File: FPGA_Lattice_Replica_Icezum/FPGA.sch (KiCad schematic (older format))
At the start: 33 parts, among them U1 iCE40HX1K-TQ144, U2 N25Q032A

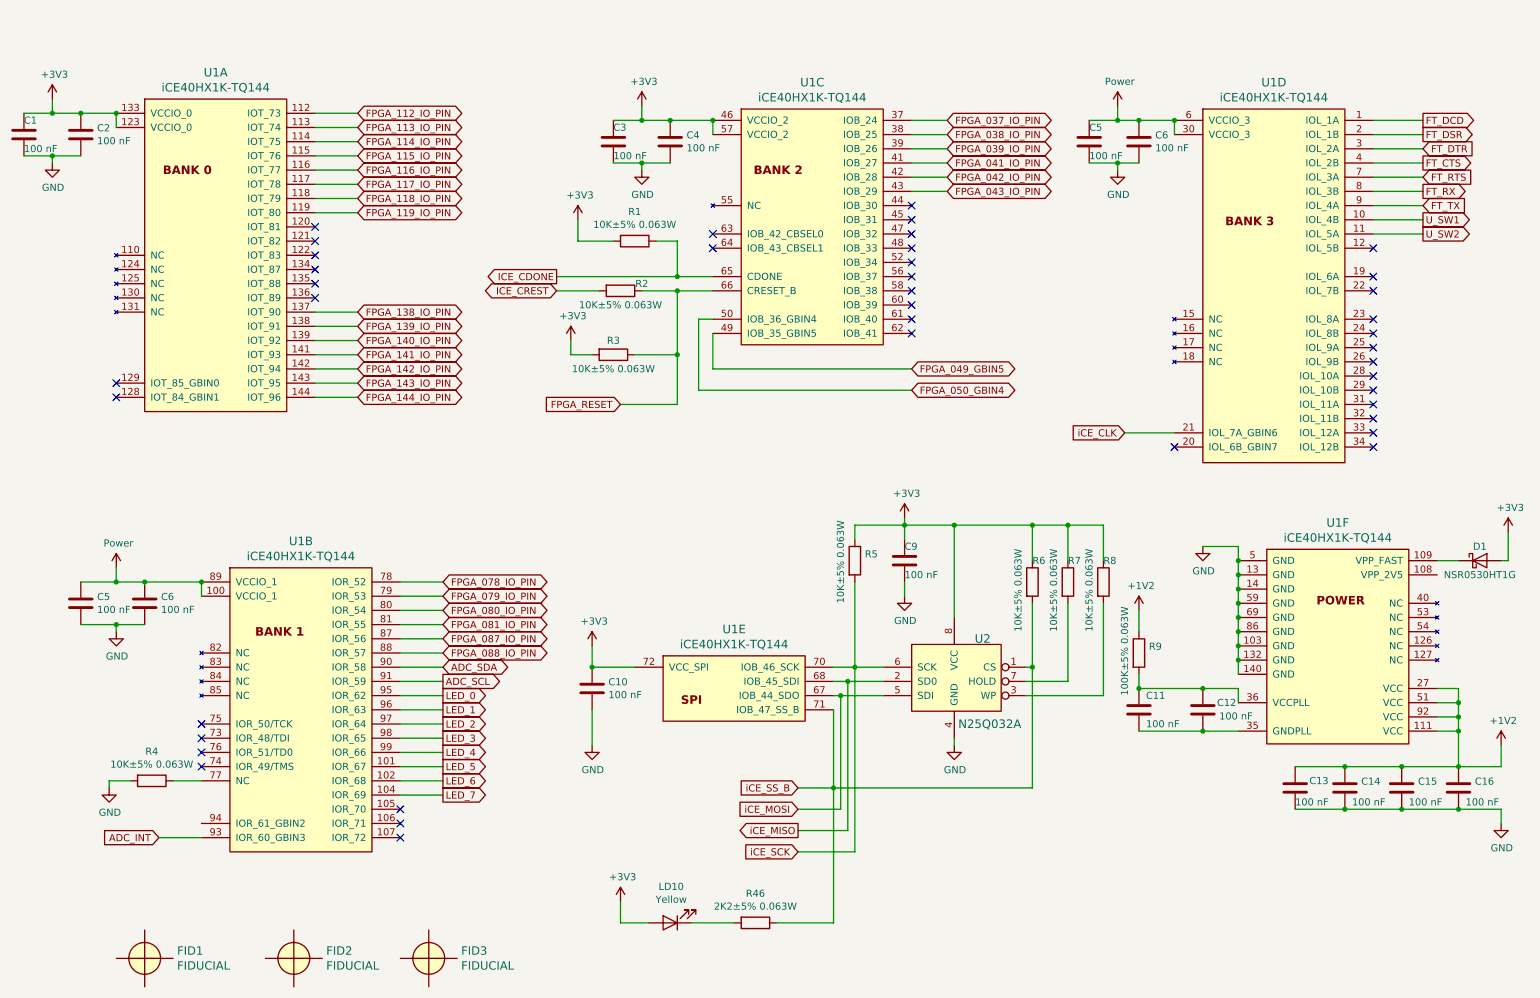
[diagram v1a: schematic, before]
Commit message: se ejecuto y se corrigio electrical rules check
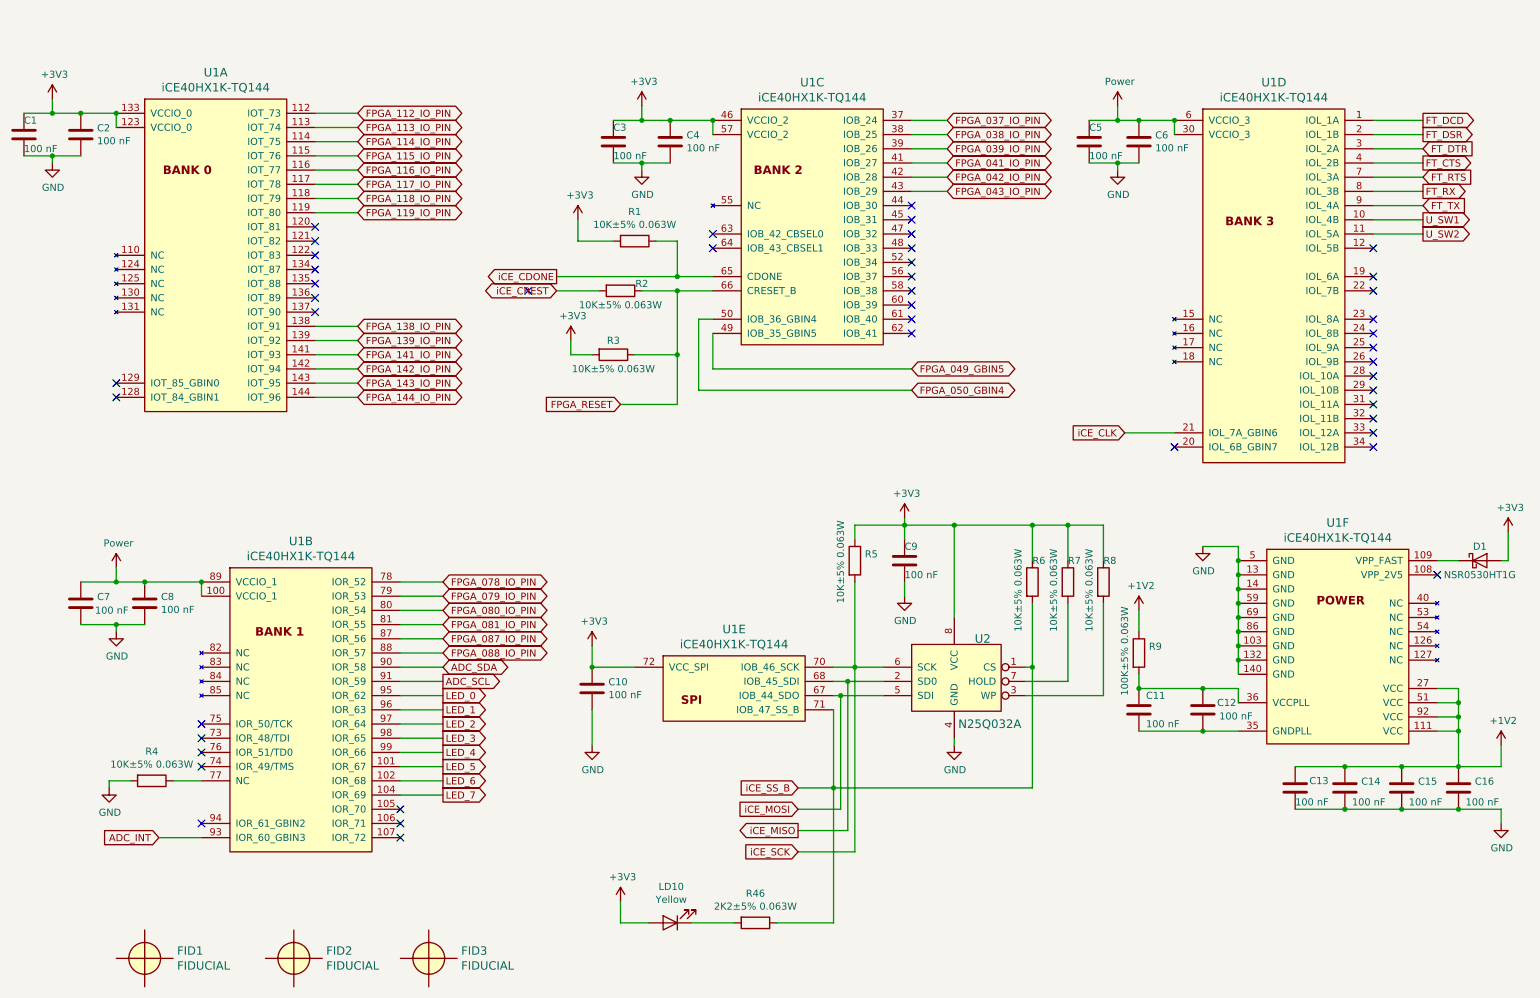
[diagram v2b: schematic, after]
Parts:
- renumbered C5 to C7, C6 to C8
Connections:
- net FPGA_140_IO_PIN is gone; now on net FPGA_139_IO_PIN: U1.139 (IOT_92)
- net FPGA_138_IO_PIN: now also U1.138 (IOT_91); no longer U1.137 (IOT_90)
- net FPGA_139_IO_PIN: no longer U1.138 (IOT_91)
- net ICE_CDONE renamed iCE_CDONE
- net ICE_CREST renamed iCE_CREST
- no-connect marks 41 -> 45
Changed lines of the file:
@@
 Text GLabel 2950 2000 2    50   BiDi ~ 0
 FPGA_119_IO_PIN
-Text GLabel 2950 2700 2    50   BiDi ~ 0
+Text GLabel 2950 2800 2    50   BiDi ~ 0
 FPGA_138_IO_PIN
-Text GLabel 2950 2800 2    50   BiDi ~ 0
+Text GLabel 2950 2900 2    50   BiDi ~ 0
 FPGA_139_IO_PIN
-Text GLabel 2950 2900 2    50   BiDi ~ 0
-FPGA_140_IO_PIN
 Text GLabel 2950 3000 2    50   BiDi ~ 0
 FPGA_141_IO_PIN
@@
 ADC_INT
 $Comp
-L icezum:Power #PWR?
+L icezum:Power #PWR0125
 U 1 1 5CFD3F9F
 P 1250 4500
-F 0 "#PWR?" H 1250 4350 50  0001 C CNN
+F 0 "#PWR0125" H 1250 4350 50  0001 C CNN
 F 1 "Power" H 1265 4673 50  0000 C CNN
 F 2 "" H 1250 4500 60  0000 C CNN
@@
 $EndComp
 $Comp
-L Device:C C5
+L Device:C C7
 U 1 1 5CFD4A6A
 P 1000 4750
-F 0 "C5" H 1115 4796 50  0000 L CNN
-F 1 "100 nF" H 1115 4705 50  0000 L CNN
+F 0 "C7" H 1115 4796 50  0000 L CNN
+F 1 "100 nF" H 1100 4700 50  0000 L CNN
 F 2 "" H 1038 4600 50  0001 C CNN
 F 3 "~" H 1000 4750 50  0001 C CNN
@@
 $EndComp
 $Comp
-L Device:C C6
+L Device:C C8
 U 1 1 5CFD4C0A
 P 1450 4750
-F 0 "C6" H 1565 4796 50  0000 L CNN
+F 0 "C8" H 1565 4796 50  0000 L CNN
 F 1 "100 nF" H 1565 4705 50  0000 L CNN
 F 2 "" H 1488 4600 50  0001 C CNN
@@
 FPGA_RESET
 Text GLabel 4350 2550 0    50   BiDi ~ 0
-ICE_CREST
+iCE_CREST
 Text GLabel 4350 2450 0    50   Output ~ 0
-ICE_CDONE
+iCE_CDONE
 $Comp
 L Device:R R2
@@
 $EndComp
 $Comp
-L icezum:+3V3 #PWR?
+L icezum:+3V3 #PWR0126
 U 1 1 5CFF6677
 P 6800 4150
-F 0 "#PWR?" H 6800 4000 50  0001 C CNN
+F 0 "#PWR0126" H 6800 4000 50  0001 C CNN
 F 1 "+3V3" H 6815 4323 50  0000 C CNN
 F 2 "" H 6800 4150 60  0000 C CNN
@@
 $EndComp
 $Comp
-L icezum:+3V3 #PWR?
+L icezum:+3V3 #PWR0127
 U 1 1 5CFF66F2
 P 4600 5050
-F 0 "#PWR?" H 4600 4900 50  0001 C CNN
+F 0 "#PWR0127" H 4600 4900 50  0001 C CNN
 F 1 "+3V3" H 4615 5223 50  0000 C CNN
 F 2 "" H 4600 5050 60  0000 C CNN
@@
 $EndComp
 $Comp
-L icezum:+3V3 #PWR?
+L icezum:+3V3 #PWR0128
 U 1 1 5CFF6BF1
 P 4800 6850
-F 0 "#PWR?" H 4800 6700 50  0001 C CNN
+F 0 "#PWR0128" H 4800 6700 50  0001 C CNN
 F 1 "+3V3" H 4815 7023 50  0000 C CNN
 F 2 "" H 4800 6850 60  0000 C CNN
@@
 iCE_SCK
 $Comp
-L power:GND #PWR?
+L power:GND #PWR0129
 U 1 1 5CFFACE6
 P 4600 5750
-F 0 "#PWR?" H 4600 5500 50  0001 C CNN
+F 0 "#PWR0129" H 4600 5500 50  0001 C CNN
 F 1 "GND" H 4605 5577 50  0000 C CNN
 F 2 "" H 4600 5750 50  0001 C CNN
@@
 $EndComp
 $Comp
-L power:GND #PWR?
+L power:GND #PWR0130
 U 1 1 5CFFB30C
 P 7150 5750
-F 0 "#PWR?" H 7150 5500 50  0001 C CNN
+F 0 "#PWR0130" H 7150 5500 50  0001 C CNN
 F 1 "GND" H 7155 5577 50  0000 C CNN
 F 2 "" H 7150 5750 50  0001 C CNN
@@
 $EndComp
 $Comp
-L power:GND #PWR?
+L power:GND #PWR0131
 U 1 1 5CFFCC0F
 P 6800 4700
-F 0 "#PWR?" H 6800 4450 50  0001 C CNN
+F 0 "#PWR0131" H 6800 4450 50  0001 C CNN
 F 1 "GND" H 6805 4527 50  0000 C CNN
 F 2 "" H 6800 4700 50  0001 C CNN
@@
 Connection ~ 1850 4600
 $Comp
-L power:GND #PWR?
+L power:GND #PWR0132
 U 1 1 5D03650F
 P 1250 4950
-F 0 "#PWR?" H 1250 4700 50  0001 C CNN
+F 0 "#PWR0132" H 1250 4700 50  0001 C CNN
 F 1 "GND" H 1255 4777 50  0000 C CNN
 F 2 "" H 1250 4950 50  0001 C CNN
@@
 	1250 4600 1450 4600
 $Comp
-L power:GND #PWR?
+L power:GND #PWR0133
 U 1 1 5D03AF49
 P 800 1650
-F 0 "#PWR?" H 800 1400 50  0001 C CNN
+F 0 "#PWR0133" H 800 1400 50  0001 C CNN
 F 1 "GND" H 805 1477 50  0000 C CNN
 F 2 "" H 800 1650 50  0001 C CNN
@@
 Wire Wire Line
 	2950 2000 2650 2000
-Wire Wire Line
-	2650 2700 2950 2700
 Wire Wire Line
 	2950 2800 2650 2800
@@
 	7100 1850 6850 1850
 $Comp
-L icezum:+3V3 #PWR?
+L icezum:+3V3 #PWR0134
 U 1 1 5D097DA0
 P 4500 2050
-F 0 "#PWR?" H 4500 1900 50  0001 C CNN
+F 0 "#PWR0134" H 4500 1900 50  0001 C CNN
 F 1 "+3V3" H 4515 2223 50  0000 C CNN
 F 2 "" H 4500 2050 60  0000 C CNN
@@
 	5200 2450 4350 2450
 $Comp
-L icezum:+3V3 #PWR?
+L icezum:+3V3 #PWR0135
 U 1 1 5D0ACF52
 P 4450 2900
-F 0 "#PWR?" H 4450 2750 50  0001 C CNN
+F 0 "#PWR0135" H 4450 2750 50  0001 C CNN
 F 1 "+3V3" H 4465 3073 50  0000 C CNN
 F 2 "" H 4450 2900 60  0000 C CNN
@@
 	5350 3250 6850 3250
 $Comp
-L power:GND #PWR?
+L power:GND #PWR0136
 U 1 1 5D0DDC54
 P 4950 1700
-F 0 "#PWR?" H 4950 1450 50  0001 C CNN
+F 0 "#PWR0136" H 4950 1450 50  0001 C CNN
 F 1 "GND" H 4955 1527 50  0000 C CNN
 F 2 "" H 4950 1700 50  0001 C CNN
@@
 $EndComp
 $Comp
-L power:GND #PWR?
+L power:GND #PWR0137
 U 1 1 5D18225B
 P 1200 6050
-F 0 "#PWR?" H 1200 5800 50  0001 C CNN
+F 0 "#PWR0137" H 1200 5800 50  0001 C CNN
 F 1 "GND" H 1205 5877 50  0000 C CNN
 F 2 "" H 1200 6050 50  0001 C CNN
@@
 $EndComp
 $Comp
-L icezum:Power #PWR?
+L icezum:Power #PWR0138
 U 1 1 5D192FB9
 P 8300 1250
-F 0 "#PWR?" H 8300 1100 50  0001 C CNN
+F 0 "#PWR0138" H 8300 1100 50  0001 C CNN
 F 1 "Power" H 8315 1423 50  0000 C CNN
 F 2 "" H 8300 1250 60  0000 C CNN
@@
 $EndComp
 $Comp
-L power:GND #PWR?
+L power:GND #PWR0139
 U 1 1 5D193C6D
 P 8300 1700
-F 0 "#PWR?" H 8300 1450 50  0001 C CNN
+F 0 "#PWR0139" H 8300 1450 50  0001 C CNN
 F 1 "GND" H 8305 1527 50  0000 C CNN
 F 2 "" H 8300 1700 50  0001 C CNN
@@
 Connection ~ 8700 1350
 $Comp
-L power:GND #PWR?
+L power:GND #PWR0140
 U 1 1 5D1C44B0
 P 8900 4350
-F 0 "#PWR?" H 8900 4100 50  0001 C CNN
+F 0 "#PWR0140" H 8900 4100 50  0001 C CNN
 F 1 "GND" H 8905 4177 50  0000 C CNN
 F 2 "" H 8900 4350 50  0001 C CNN
@@
 $EndComp
 $Comp
-L icezum:+1V2 #PWR?
+L icezum:+1V2 #PWR0141
 U 1 1 5D1C6F5E
 P 8450 4800
-F 0 "#PWR?" H 8450 4650 50  0001 C CNN
+F 0 "#PWR0141" H 8450 4650 50  0001 C CNN
 F 1 "+1V2" H 8465 4973 50  0000 C CNN
 F 2 "" H 8450 4800 60  0000 C CNN
@@
 $EndComp
 $Comp
-L power:GND #PWR?
+L power:GND #PWR0142
 U 1 1 5D1C9C8A
 P 11000 6300
-F 0 "#PWR?" H 11000 6050 50  0001 C CNN
+F 0 "#PWR0142" H 11000 6050 50  0001 C CNN
 F 1 "GND" H 11005 6127 50  0000 C CNN
 F 2 "" H 11000 6300 50  0001 C CNN
@@
 $EndComp
 $Comp
-L icezum:+1V2 #PWR?
+L icezum:+1V2 #PWR0143
 U 1 1 5D1CAE01
 P 11000 5750
-F 0 "#PWR?" H 11000 5600 50  0001 C CNN
+F 0 "#PWR0143" H 11000 5600 50  0001 C CNN
 F 1 "+1V2" H 11015 5923 50  0000 C CNN
 F 2 "" H 11000 5750 60  0000 C CNN
@@
 $EndComp
 $Comp
-L icezum:+3V3 #PWR?
+L icezum:+3V3 #PWR0144
 U 1 1 5D1CCFC9
 P 11050 4250
-F 0 "#PWR?" H 11050 4100 50  0001 C CNN
+F 0 "#PWR0144" H 11050 4100 50  0001 C CNN
 F 1 "+3V3" H 11065 4423 50  0000 C CNN
 F 2 "" H 11050 4250 60  0000 C CNN
@@
 	1    0    0    -1
 $EndComp
+NoConn ~ 2650 2700
+NoConn ~ 4150 2550
+NoConn ~ 10550 4550
+NoConn ~ 1850 6300
 $EndSCHEMATC

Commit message: se comenzo asignacion de footprints
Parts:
- C1, C10, C2, C3, C4, C5, C6, C7, C8, C9: footprint (none) -> footprints:C_0402
- C11: footprint (none) -> footprints:C_0603
- D1: footprint (none) -> footprints:SOD-323
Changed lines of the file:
@@
 F 0 "U1" H 1950 1587 60  0000 C CNN
 F 1 "iCE40HX1K-TQ144" H 1950 1481 60  0000 C CNN
-F 2 "" H 1600 100 60  0000 C CNN
+F 2 "" H 1600 100 60  0001 C CNN
 F 3 "" H 1600 100 60  0000 C CNN
 	1    1250 1300
@@
 F 0 "U1" H 2550 4887 60  0000 C CNN
 F 1 "iCE40HX1K-TQ144" H 2550 4781 60  0000 C CNN
-F 2 "" H 2200 3400 60  0000 C CNN
+F 2 "" H 2200 3400 60  0001 C CNN
 F 3 "" H 2200 3400 60  0000 C CNN
 	2    1850 4600
@@
 F 0 "U1" H 6150 1617 60  0000 C CNN
 F 1 "iCE40HX1K-TQ144" H 6150 1511 60  0000 C CNN
-F 2 "" H 5800 150 60  0000 C CNN
+F 2 "" H 5800 150 60  0001 C CNN
 F 3 "" H 5800 150 60  0000 C CNN
 	3    5450 1350
@@
 F 0 "U1" H 9400 1617 60  0000 C CNN
 F 1 "iCE40HX1K-TQ144" H 9400 1511 60  0000 C CNN
-F 2 "" H 9050 150 60  0000 C CNN
+F 2 "" H 9050 150 60  0001 C CNN
 F 3 "" H 9050 150 60  0000 C CNN
 	4    8700 1350
@@
 F 0 "U1" H 5600 5467 60  0000 C CNN
 F 1 "iCE40HX1K-TQ144" H 5600 5361 60  0000 C CNN
-F 2 "" H 5250 4000 60  0000 C CNN
+F 2 "" H 5250 4000 60  0001 C CNN
 F 3 "" H 5250 4000 60  0000 C CNN
 	5    4900 5200
@@
 F 0 "U1" H 9850 4717 60  0000 C CNN
 F 1 "iCE40HX1K-TQ144" H 9850 4611 60  0000 C CNN
-F 2 "" H 9500 3250 60  0000 C CNN
+F 2 "" H 9500 3250 60  0001 C CNN
 F 3 "" H 9500 3250 60  0000 C CNN
 	6    9150 4450
@@
 F 0 "C1" H 600 1550 50  0000 L CNN
 F 1 "100 nF" H 600 1350 50  0000 L CNN
-F 2 "" H 638 1300 50  0001 C CNN
+F 2 "footprints:C_0402" H 638 1300 50  0001 C CNN
 F 3 "~" H 600 1450 50  0001 C CNN
 	1    600  1450
@@
 F 0 "C2" H 1115 1496 50  0000 L CNN
 F 1 "100 nF" H 1115 1405 50  0000 L CNN
-F 2 "" H 1038 1300 50  0001 C CNN
+F 2 "footprints:C_0402" H 1038 1300 50  0001 C CNN
 F 3 "~" H 1000 1450 50  0001 C CNN
 	1    1000 1450
@@
 F 0 "C3" H 4750 1600 50  0000 L CNN
 F 1 "100 nF" H 4750 1400 50  0000 L CNN
-F 2 "" H 4788 1350 50  0001 C CNN
+F 2 "footprints:C_0402" H 4788 1350 50  0001 C CNN
 F 3 "~" H 4750 1500 50  0001 C CNN
 	1    4750 1500
@@
 F 0 "C4" H 5265 1546 50  0000 L CNN
 F 1 "100 nF" H 5265 1455 50  0000 L CNN
-F 2 "" H 5188 1350 50  0001 C CNN
+F 2 "footprints:C_0402" H 5188 1350 50  0001 C CNN
 F 3 "~" H 5150 1500 50  0001 C CNN
 	1    5150 1500
@@
 F 0 "C7" H 1115 4796 50  0000 L CNN
 F 1 "100 nF" H 1100 4700 50  0000 L CNN
-F 2 "" H 1038 4600 50  0001 C CNN
+F 2 "footprints:C_0402" H 1038 4600 50  0001 C CNN
 F 3 "~" H 1000 4750 50  0001 C CNN
 	1    1000 4750
@@
 F 0 "C8" H 1565 4796 50  0000 L CNN
 F 1 "100 nF" H 1565 4705 50  0000 L CNN
-F 2 "" H 1488 4600 50  0001 C CNN
+F 2 "footprints:C_0402" H 1488 4600 50  0001 C CNN
 F 3 "~" H 1450 4750 50  0001 C CNN
 	1    1450 4750
@@
 F 0 "U2" H 7350 5400 60  0000 C CNN
 F 1 "N25Q032A" H 7400 4800 60  0000 C CNN
-F 2 "" H 7180 5300 60  0000 C CNN
+F 2 "" H 7180 5300 60  0001 C CNN
 F 3 "" H 7180 5300 60  0000 C CNN
 	1    6650 5200
@@
 F 0 "C10" H 4715 5396 50  0000 L CNN
 F 1 "100 nF" H 4715 5305 50  0000 L CNN
-F 2 "" H 4638 5200 50  0001 C CNN
+F 2 "footprints:C_0402" H 4638 5200 50  0001 C CNN
 F 3 "~" H 4600 5350 50  0001 C CNN
 	1    4600 5350
@@
 F 0 "C9" H 6800 4550 50  0000 L CNN
 F 1 "100 nF" H 6800 4350 50  0000 L CNN
-F 2 "" H 6838 4300 50  0001 C CNN
+F 2 "footprints:C_0402" H 6838 4300 50  0001 C CNN
 F 3 "~" H 6800 4450 50  0001 C CNN
 	1    6800 4450
@@
 F 0 "C5" H 8100 1600 50  0000 L CNN
 F 1 "100 nF" H 8100 1400 50  0000 L CNN
-F 2 "" H 8138 1350 50  0001 C CNN
+F 2 "footprints:C_0402" H 8138 1350 50  0001 C CNN
 F 3 "~" H 8100 1500 50  0001 C CNN
 	1    8100 1500
@@
 F 0 "C6" H 8565 1546 50  0000 L CNN
 F 1 "100 nF" H 8565 1455 50  0000 L CNN
-F 2 "" H 8488 1350 50  0001 C CNN
+F 2 "footprints:C_0402" H 8488 1350 50  0001 C CNN
 F 3 "~" H 8450 1500 50  0001 C CNN
 	1    8450 1500
@@
 F 0 "C11" H 8500 5600 50  0000 L CNN
 F 1 "100 nF" H 8500 5400 50  0000 L CNN
-F 2 "" H 8488 5350 50  0001 C CNN
+F 2 "footprints:C_0603" H 8488 5350 50  0001 C CNN
 F 3 "~" H 8450 5500 50  0001 C CNN
 	1    8450 5500
@@
 F 0 "D1" H 10850 4550 50  0000 C CNN
 F 1 "NSR0530HT1G" H 10850 4350 50  0000 C CNN
-F 2 "" H 10850 4450 50  0001 C CNN
+F 2 "footprints:SOD-323" H 10850 4450 50  0001 C CNN
 F 3 "~" H 10850 4450 50  0001 C CNN
 	1    10850 4450
@@
 F 0 "FID1" H 1678 7303 59  0000 L CNN
 F 1 "FIDUCIAL" H 1678 7198 59  0000 L CNN
-F 2 "" H 1450 7250 157 0000 C CNN
+F 2 "" H 1450 7250 157 0001 C CNN
 F 3 "" H 1450 7250 157 0000 C CNN
 	1    1450 7250
@@
 F 0 "FID2" H 2728 7303 59  0000 L CNN
 F 1 "FIDUCIAL" H 2728 7198 59  0000 L CNN
-F 2 "" H 2500 7250 157 0000 C CNN
+F 2 "" H 2500 7250 157 0001 C CNN
 F 3 "" H 2500 7250 157 0000 C CNN
 	1    2500 7250
@@
 F 0 "FID3" H 3678 7303 59  0000 L CNN
 F 1 "FIDUCIAL" H 3678 7198 59  0000 L CNN
-F 2 "" H 3450 7250 157 0000 C CNN
+F 2 "" H 3450 7250 157 0001 C CNN
 F 3 "" H 3450 7250 157 0000 C CNN
 	1    3450 7250
